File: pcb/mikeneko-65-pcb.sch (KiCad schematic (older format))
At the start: 18 parts, among them J1 JST SH 4-pin, J2 AVR-ISP-6, SW1 Reset, U1 SRV05-4, U2 ATmega32U4-AU, Y1 16MHz

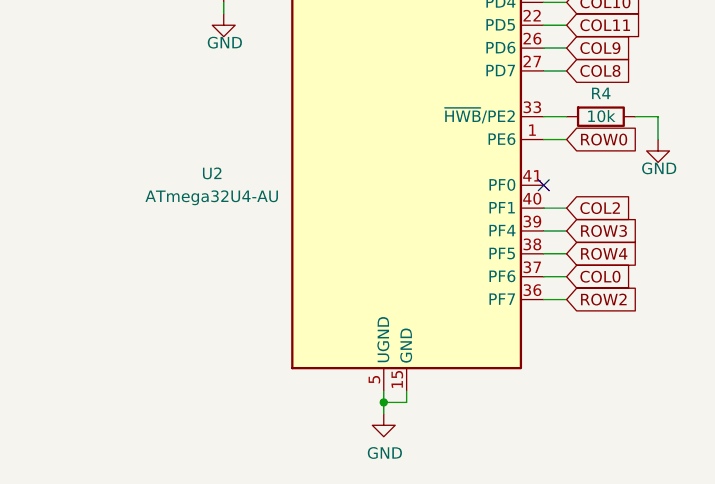
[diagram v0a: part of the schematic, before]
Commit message: 回路図のmcuをatmega32u4-muに変更。
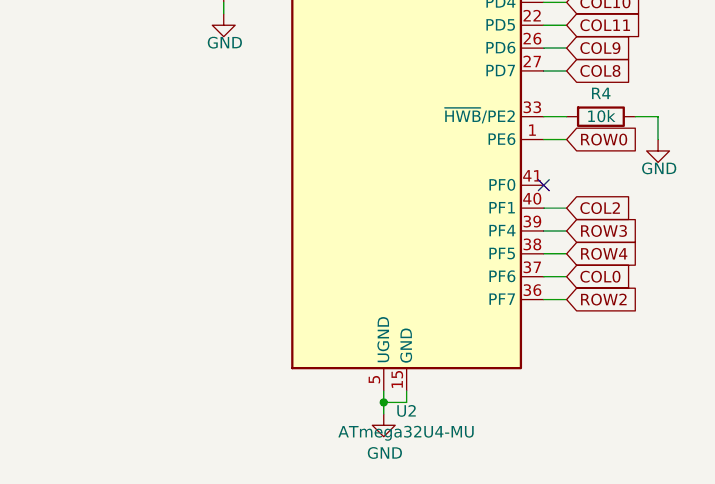
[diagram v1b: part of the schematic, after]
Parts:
- removed U2: ATmega32U4-AU, Package_QFP:TQFP-44_10x10mm_P0.8mm, symbol MCU_Microchip_ATmega:ATmega32U4-AU
- added U2: ATmega32U4-MU, Package_DFN_QFN:QFN-44-1EP_7x7mm_P0.5mm_EP5.2x5.2mm, symbol MCU_Microchip_ATmega:ATmega32U4-MU
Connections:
- net +5V: now also U2.14 (VCC), U2.2 (UVCC), U2.24 (AVCC), U2.34 (VCC), U2.44 (AVCC), U2.7 (VBUS)
- net COL0: now also U2.37 (PF6)
- net COL1: now also U2.8 (PB0)
- net COL10: now also U2.25 (PD4)
- net COL11: now also U2.22 (PD5)
- net COL12: now also U2.21 (PD3)
- net COL13: now also U2.20 (PD2)
- net COL14: now also U2.19 (PD1)
- net COL15: now also U2.18 (PD0)
- net COL2: now also U2.40 (PF1)
- net COL3: now also U2.32 (PC7)
- net COL4: now also U2.31 (PC6)
- net COL5: now also U2.30 (PB6)
- net COL6: now also U2.29 (PB5)
- net COL7: now also U2.28 (PB4)
- net COL8: now also U2.27 (PD7)
- net COL9: now also U2.26 (PD6)
- net GND: now also U2.15 (GND), U2.23 (GND), U2.35 (GND), U2.43 (GND), U2.45 (GND), U2.5 (UGND)
- net MCU_D+: now also U2.4 (D+)
- net MCU_D-: now also U2.3 (D-)
- net MISO: now also U2.11 (PB3)
- net MOSI: now also U2.10 (PB2)
- net RESET: now also U2.13 (~RESET)
- net ROW0: now also U2.1 (PE6)
- net ROW1: now also U2.12 (PB7)
- net ROW2: now also U2.36 (PF7)
- net ROW3: now also U2.39 (PF4)
- net ROW4: now also U2.38 (PF5)
- net SCK: now also U2.9 (PB1)
- net XTAL1: now also U2.17 (XTAL1)
- net XTAL2: now also U2.16 (XTAL2)
- net at R4.2: now also U2.33 (~HWB~/PE2)
- net at C7.1: now also U2.6 (UCAP)
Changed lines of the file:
@@
 D+
-$Comp
-L MCU_Microchip_ATmega:ATmega32U4-AU U2
-U 1 1 5F26004F
-P 2300 5050
-F 0 "U2" H 1450 4200 50  0000 C CNN
-F 1 "ATmega32U4-AU" H 1450 4100 50  0000 C CNN
-F 2 "Package_QFP:TQFP-44_10x10mm_P0.8mm" H 2300 5050 50  0001 C CIN
-F 3 "http://ww1.microchip.com/downloads/en/DeviceDoc/Atmel-7766-8-bit-AVR-ATmega16U4-32U4_Datasheet.pdf" H 2300 5050 50  0001 C CNN
-F 4 "C44854" H 2300 5050 50  0001 C CNN "LCSC Part #"
-	1    2300 5050
-	1    0    0    -1
-$EndComp
 $Comp
 L Device:R R3
@@
 	1    0    0    -1
 $EndComp
+$Comp
+L MCU_Microchip_ATmega:ATmega32U4-MU U2
+U 1 1 61D221A9
+P 2300 5050
+F 0 "U2" H 2300 3161 50  0000 C CNN
+F 1 "ATmega32U4-MU" H 2300 3070 50  0000 C CNN
+F 2 "Package_DFN_QFN:QFN-44-1EP_7x7mm_P0.5mm_EP5.2x5.2mm" H 2300 5050 50  0001 C CIN
+F 3 "http://ww1.microchip.com/downloads/en/DeviceDoc/Atmel-7766-8-bit-AVR-ATmega16U4-32U4_Datasheet.pdf" H 2300 5050 50  0001 C CNN
+	1    2300 5050
+	1    0    0    -1
+$EndComp

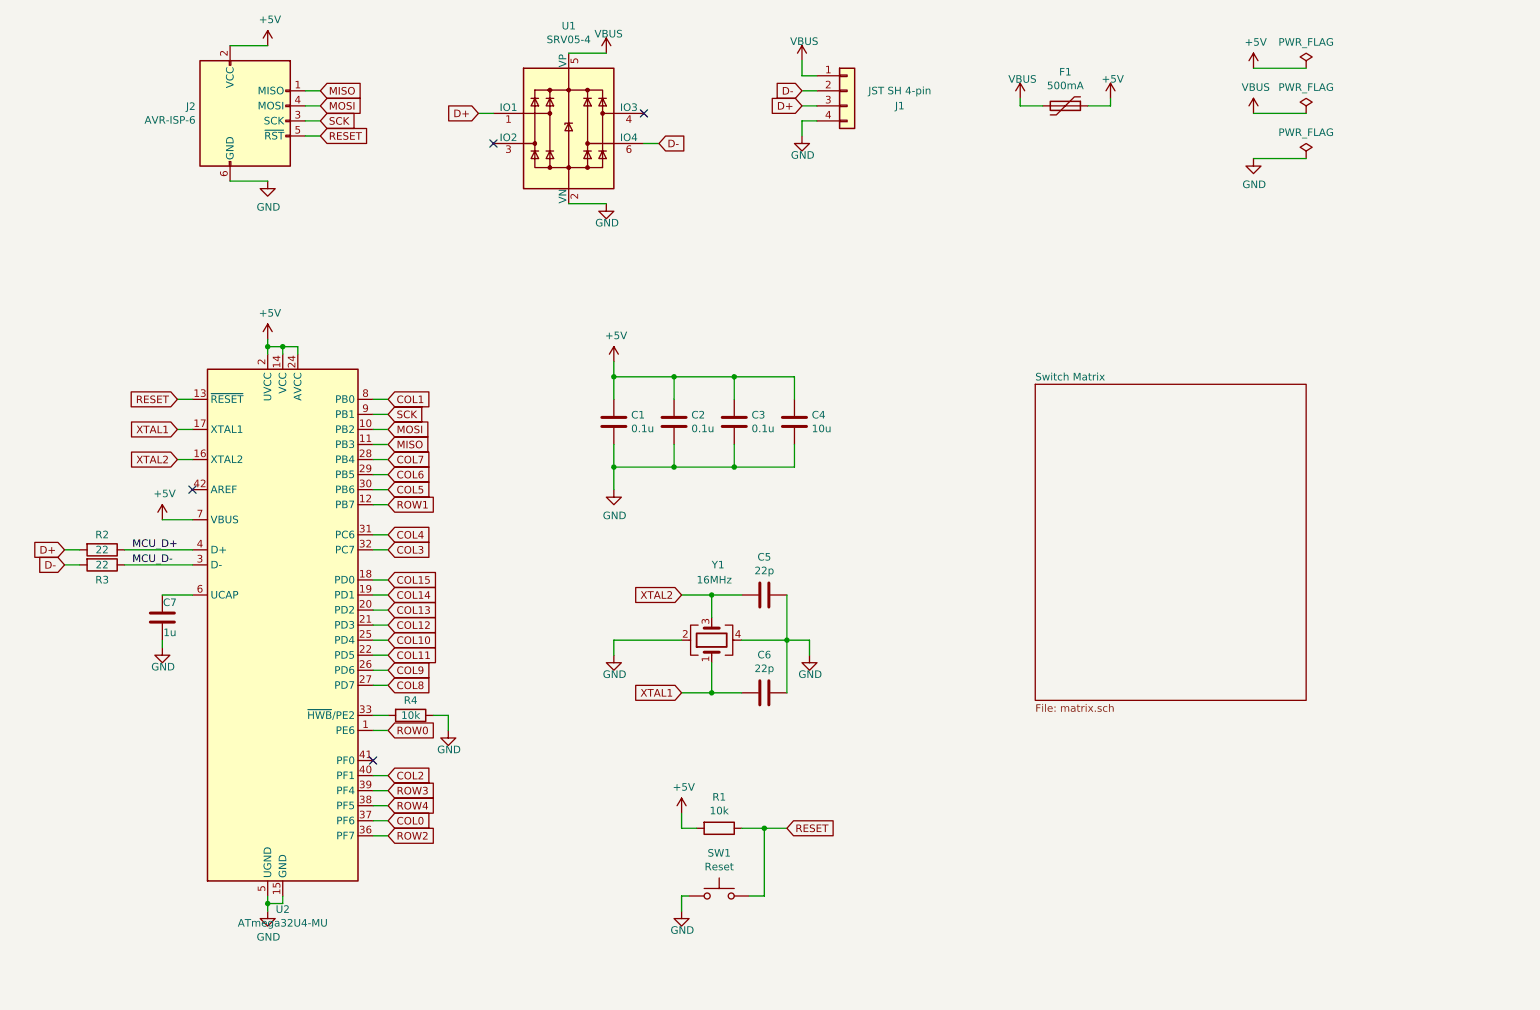
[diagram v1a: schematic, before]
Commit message: ソケットに対応。
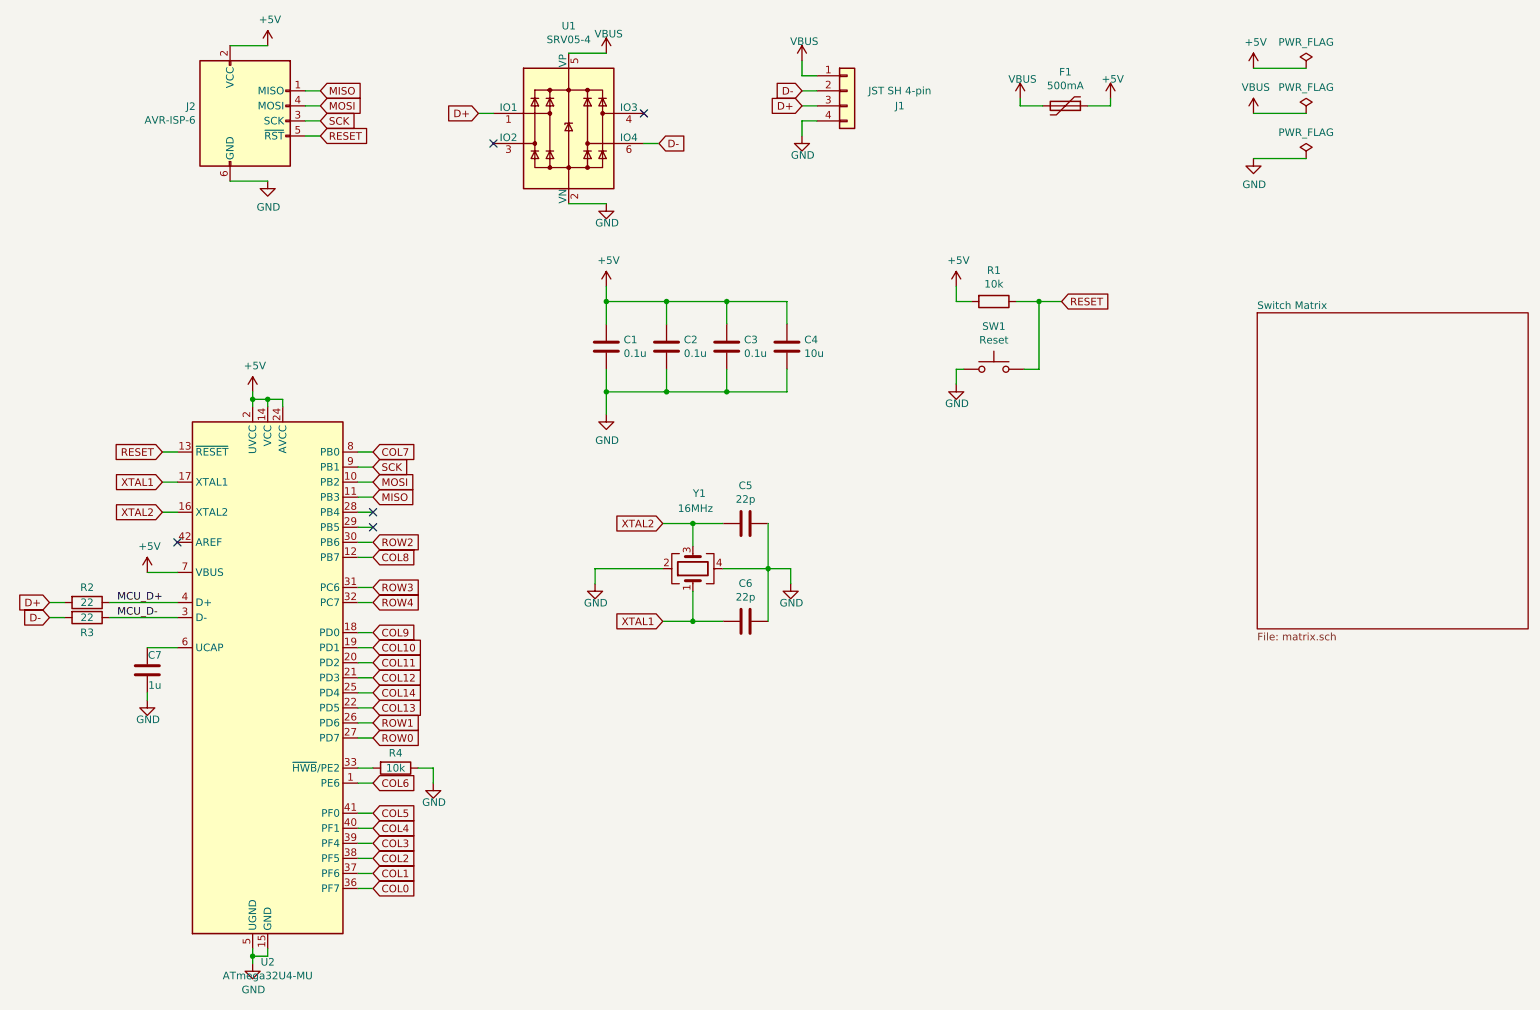
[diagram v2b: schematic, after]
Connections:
- net COL15 is gone; now on net COL9: U2.18 (PD0)
- net COL0: now also U2.36 (PF7); no longer U2.37 (PF6)
- net COL1: now also U2.37 (PF6); no longer U2.8 (PB0)
- net COL10: now also U2.19 (PD1); no longer U2.25 (PD4)
- net COL11: now also U2.20 (PD2); no longer U2.22 (PD5)
- net COL13: now also U2.22 (PD5); no longer U2.20 (PD2)
- net COL14: now also U2.25 (PD4); no longer U2.19 (PD1)
- net COL2: now also U2.38 (PF5); no longer U2.40 (PF1)
- net COL3: now also U2.39 (PF4); no longer U2.32 (PC7)
- net COL4: now also U2.40 (PF1); no longer U2.31 (PC6)
- net COL5: now also U2.41 (PF0); no longer U2.30 (PB6)
- net COL6: now also U2.1 (PE6); no longer U2.29 (PB5)
- net COL7: now also U2.8 (PB0); no longer U2.28 (PB4)
- net COL8: now also U2.12 (PB7); no longer U2.27 (PD7)
- net COL9: no longer U2.26 (PD6)
- net ROW0: now also U2.27 (PD7); no longer U2.1 (PE6)
- net ROW1: now also U2.26 (PD6); no longer U2.12 (PB7)
- net ROW2: now also U2.30 (PB6); no longer U2.36 (PF7)
- net ROW3: now also U2.31 (PC6); no longer U2.39 (PF4)
- net ROW4: now also U2.32 (PC7); no longer U2.38 (PF5)
- no-connect marks 4 -> 5
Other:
- moved on the sheet: C1, C2, C3, C4, C5, C6, C7, R1, R2, R3, R4, SW1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

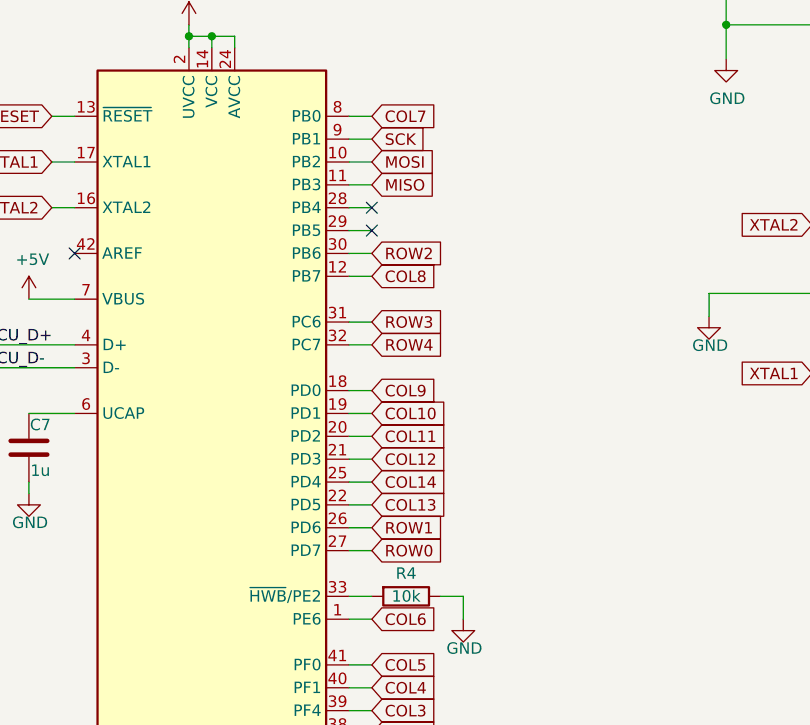
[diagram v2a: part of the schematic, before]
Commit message: 配線を更新。
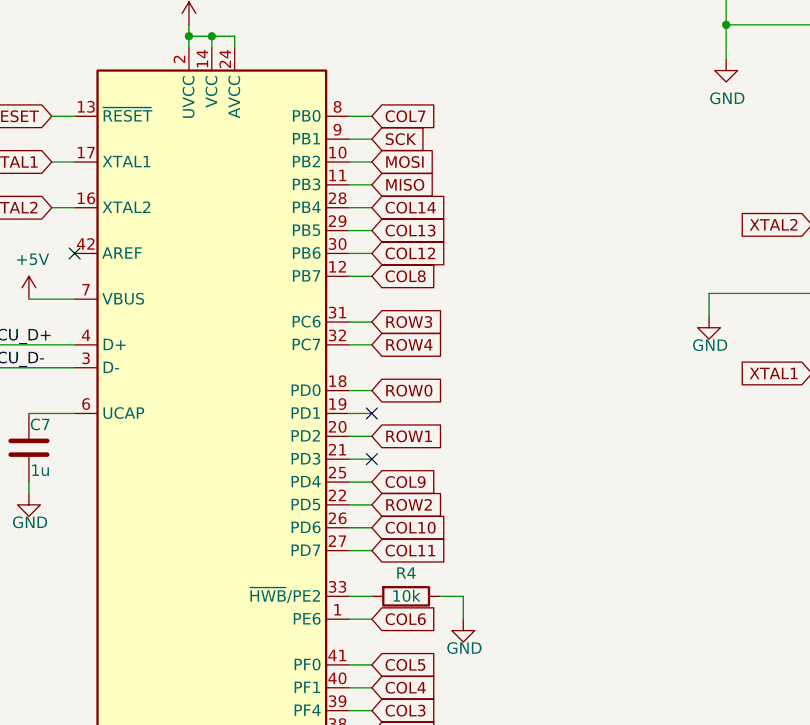
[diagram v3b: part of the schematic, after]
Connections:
- net COL10: now also U2.26 (PD6); no longer U2.19 (PD1)
- net COL11: now also U2.27 (PD7); no longer U2.20 (PD2)
- net COL12: now also U2.30 (PB6); no longer U2.21 (PD3)
- net COL13: now also U2.29 (PB5); no longer U2.22 (PD5)
- net COL14: now also U2.28 (PB4); no longer U2.25 (PD4)
- net COL9: now also U2.25 (PD4); no longer U2.18 (PD0)
- net ROW0: now also U2.18 (PD0); no longer U2.27 (PD7)
- net ROW1: now also U2.20 (PD2); no longer U2.26 (PD6)
- net ROW2: now also U2.22 (PD5); no longer U2.30 (PB6)
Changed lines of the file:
@@
 EESchema Schematic File Version 4
-LIBS:mikeneko-65-pcb-cache
 EELAYER 30 0
 EELAYER END
@@
 Text GLabel 2900 4100 2    50   Input ~ 0
 MOSI
-Text GLabel 2900 5200 2    50   Input ~ 0
+Text GLabel 2900 5700 2    50   Input ~ 0
 COL10
+Text GLabel 2900 5800 2    50   Input ~ 0
+COL11
+Text GLabel 2900 4500 2    50   Input ~ 0
+COL12
+Text GLabel 2900 4400 2    50   Input ~ 0
+COL13
+Text GLabel 2900 4300 2    50   Input ~ 0
+COL14
 Text GLabel 2900 5300 2    50   Input ~ 0
-COL11
-Text GLabel 2900 5400 2    50   Input ~ 0
-COL12
+ROW1
+Text GLabel 2900 5100 2    50   Input ~ 0
+ROW0
 Text GLabel 2900 5600 2    50   Input ~ 0
-COL13
-Text GLabel 2900 5500 2    50   Input ~ 0
-COL14
-Text GLabel 2900 5700 2    50   Input ~ 0
-ROW1
-Text GLabel 2900 5800 2    50   Input ~ 0
-ROW0
-Text GLabel 2900 4500 2    50   Input ~ 0
 ROW2
 Text GLabel 2900 4800 2    50   Input ~ 0
@@
 	2800 3900 2900 3900
 Wire Wire Line
-	2900 4000 2800 4000
-Wire Wire Line
-	2800 4100 2900 4100
-Wire Wire Line
-	2900 4200 2800 4200
-Wire Wire Line
-	2800 4300 2900 4300
-Wire Wire Line
 	2900 4400 2800 4400
 Wire Wire Line
@@
 	1    0    0    -1
 $EndComp
-Text GLabel 2900 5100 2    50   Input ~ 0
+Text GLabel 2900 5500 2    50   Input ~ 0
 COL9
 Wire Wire Line
@@
 Wire Wire Line
 	2900 6300 2800 6300
-NoConn ~ 2900 4300
-NoConn ~ 2900 4400
+Wire Wire Line
+	2900 4300 2800 4300
+NoConn ~ 2900 5200
+NoConn ~ 2900 5400
+Wire Wire Line
+	2900 4000 2800 4000
+Wire Wire Line
+	2900 4100 2800 4100
+Wire Wire Line
+	2900 4200 2800 4200
 $EndSCHEMATC
